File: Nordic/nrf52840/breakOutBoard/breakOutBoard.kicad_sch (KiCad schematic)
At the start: 24 parts, among them J1 Conn_ARM_JTAG_SWD_10, U1 NRF52840-QFAA-R7, Y1 Crystal, Y2 ECS-327MVATX-3-CN-TR3

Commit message: projects
Update projects
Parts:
- removed Y1: Crystal, Crystal:Crystal_SMD_Qantek_QC5CB-2Pin_5x3.2mm, symbol Device:Crystal
- added Y1: ECS-320-8-37B-CKY-TR, User_Footprint:XTAL_ECS-160-9-37-CKM-TR, symbol _Misc_Symbols:ECS-320-8-37B-CKY-TR
- renumbered C18 to J2
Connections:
- net GND: now also C10.1, C9.1, J2.2, J2.4, Y1.2 (GND), Y1.4 (GND__1); no longer C10.2, C9.2
- net P0.02: now also J2.26
- net P0.03: now also J2.24
- net P0.04: now also J2.5
- net P0.05: now also J2.7
- net P0.07: now also J2.9
- net P0.08: now also J2.6
- net P0.09: now also J2.31
- net P0.11: now also J2.13
- net P0.12: now also J2.10
- net P0.13: now also J2.12
- net P0.14: now also J2.14
- net P0.17: now also J2.15
- net P0.18: now also J2.16
- net P0.19: now also J2.17
- net P0.20: now also J2.19
- net P0.21: now also J2.21
- net P0.22: now also J2.23
- net P0.23: now also J2.25
- net P0.24: now also J2.27
- net P0.28: now also J2.28
- net P0.29: now also J2.18
- net P0.30: now also J2.20
- net P0.31: now also J2.22
- net P1.00: now also J2.29
- net P1.08: now also J2.8
- net P1.09: now also J2.11
- net VDD: now also J2.1, J2.3
- net XC1: now reaches U1.36 (XC2)
- net XC1: now also C10.2, Y1.1 (IN/OUT); no longer C10.1
- net XC2: now reaches U1.35 (XC1)
- net XC2: now also C9.2, Y1.3 (OUT/IN); no longer C9.1
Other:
- moved on the sheet: C10, C9

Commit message: antenna
Implementing antenna layout
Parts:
- added C3: 1.0pF, Capacitor_SMD:C_0402_1005Metric_Pad0.74x0.62mm_HandSolder, symbol Device:C
- added E1: 2450AT18A0100001E, User_Footprint:XCVR_2450AT18A0100001E, symbol _Misc_Symbols:2450AT18A0100001E
- added L5: 2.7nH, Inductor_SMD:L_0402_1005Metric_Pad0.77x0.64mm_HandSolder, symbol Device:L
- added L6: 3.9nH, Inductor_SMD:L_0402_1005Metric_Pad0.77x0.64mm_HandSolder, symbol Device:L
- C14: value 1pF -> 1.0pF
- C15: value 1p2F -> 1.2pF
- L1: value 4n7H -> 4.7nH
- L2: value 2n2H -> 2.2nH
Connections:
- net GND: now also L5.2
- net P0.09: now also J2.32; no longer J2.31
- net P1.15: now also J2.30
- net at L2.2: now also C3.1
- new net: C3.2, L5.1, L6.1
- new net: E1.1, L6.2
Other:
- note added: "50 0hm"

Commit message: layout
changed Layout
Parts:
- C1, C10, C11, C12, C13, C14, C15, C16, C17, C19, C2, C3, C4, C5, C6, C9: footprint Capacitor_SMD:C_0402_1005Metric_Pad0.74x0.62mm_HandSolder -> Capacitor_SMD:C_0201_0603Metric
- L1, L2, L3, L4, L5, L6: footprint Inductor_SMD:L_0402_1005Metric_Pad0.77x0.64mm_HandSolder -> Inductor_SMD:L_0201_0603Metric
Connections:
- net GND: now also J2.44, J2.46, J2.48, J2.50, J2.52
- net P0.02: now also J2.34; no longer J2.26
- net P0.03: now also J2.26; no longer J2.24
- net P0.10: now also J2.31
- net P0.28: now also J2.24; no longer J2.28
- net P0.29: now also J2.22; no longer J2.18
- net P0.31: now also J2.18; no longer J2.22
- net VDD: now also J2.43, J2.45, J2.47, J2.49, J2.51
- no-connect marks 5 -> 15

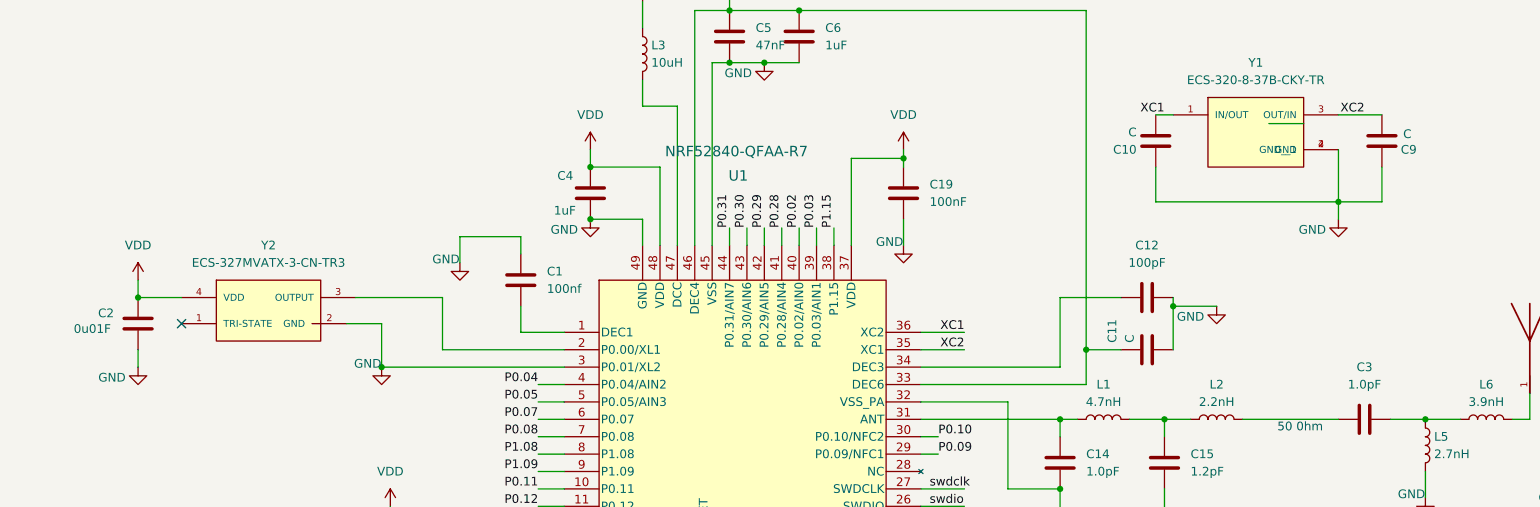
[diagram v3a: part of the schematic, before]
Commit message: Update
Change some footprints and update RF trace
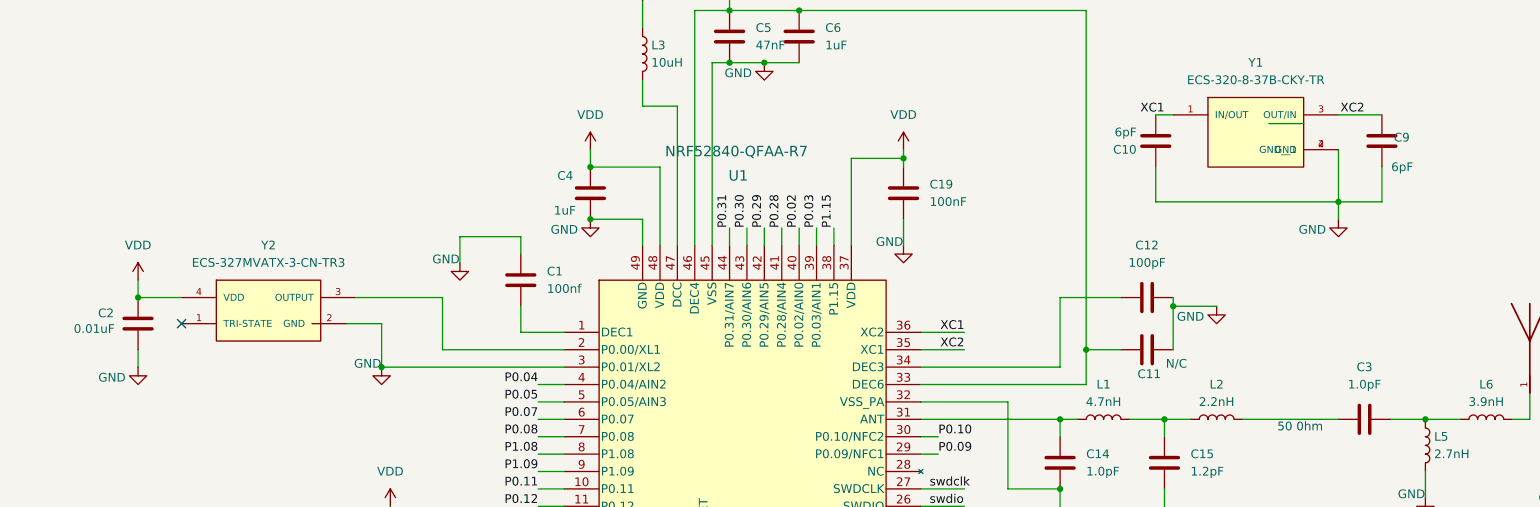
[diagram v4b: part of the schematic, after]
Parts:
- C10, C9: value C -> 6pF
- C11: value C -> N/C
- C2: value 0u01F -> 0.01uF
- L3: footprint Inductor_SMD:L_0201_0603Metric -> Inductor_SMD:L_0603_1608Metric
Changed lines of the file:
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@@
 			)
 		)
-		(property "Value" "C"
+		(property "Value" "6pF"
 			(at 199.136 59.69 0)
 			(effects
@@
 			)
 		)
-		(property "Footprint" "Inductor_SMD:L_0201_0603Metric"
+		(property "Footprint" "Inductor_SMD:L_0603_1608Metric"
 			(at 127 48.26 0)
 			(effects
@@
 		(dnp no)
 		(property "Reference" "C9"
-			(at 240.03 62.23 0)
-			(effects
-				(font
-					(size 1.27 1.27)
-				)
-				(justify left)
-			)
-		)
-		(property "Value" "C"
-			(at 239.268 59.944 0)
+			(at 239.014 60.452 0)
+			(effects
+				(font
+					(size 1.27 1.27)
+				)
+				(justify left)
+			)
+		)
+		(property "Value" "6pF"
+			(at 239.522 64.77 0)
 			(effects
 				(font
@@
 		(dnp no)
 		(property "Reference" "C11"
-			(at 195.58 90.424 0)
-			(effects
-				(font
-					(size 1.27 1.27)
-				)
-				(justify left)
-			)
-		)
-		(property "Value" "C"
-			(at 198.12 90.424 0)
+			(at 202.692 94.996 90)
+			(effects
+				(font
+					(size 1.27 1.27)
+				)
+				(justify left)
+			)
+		)
+		(property "Value" "N/C"
+			(at 206.502 93.472 90)
 			(effects
 				(font
@@
 			)
 		)
-		(property "Value" "0u01F"
+		(property "Value" "0.01uF"
 			(at 43.942 88.392 0)
 			(effects
